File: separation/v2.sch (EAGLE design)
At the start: 6 parts

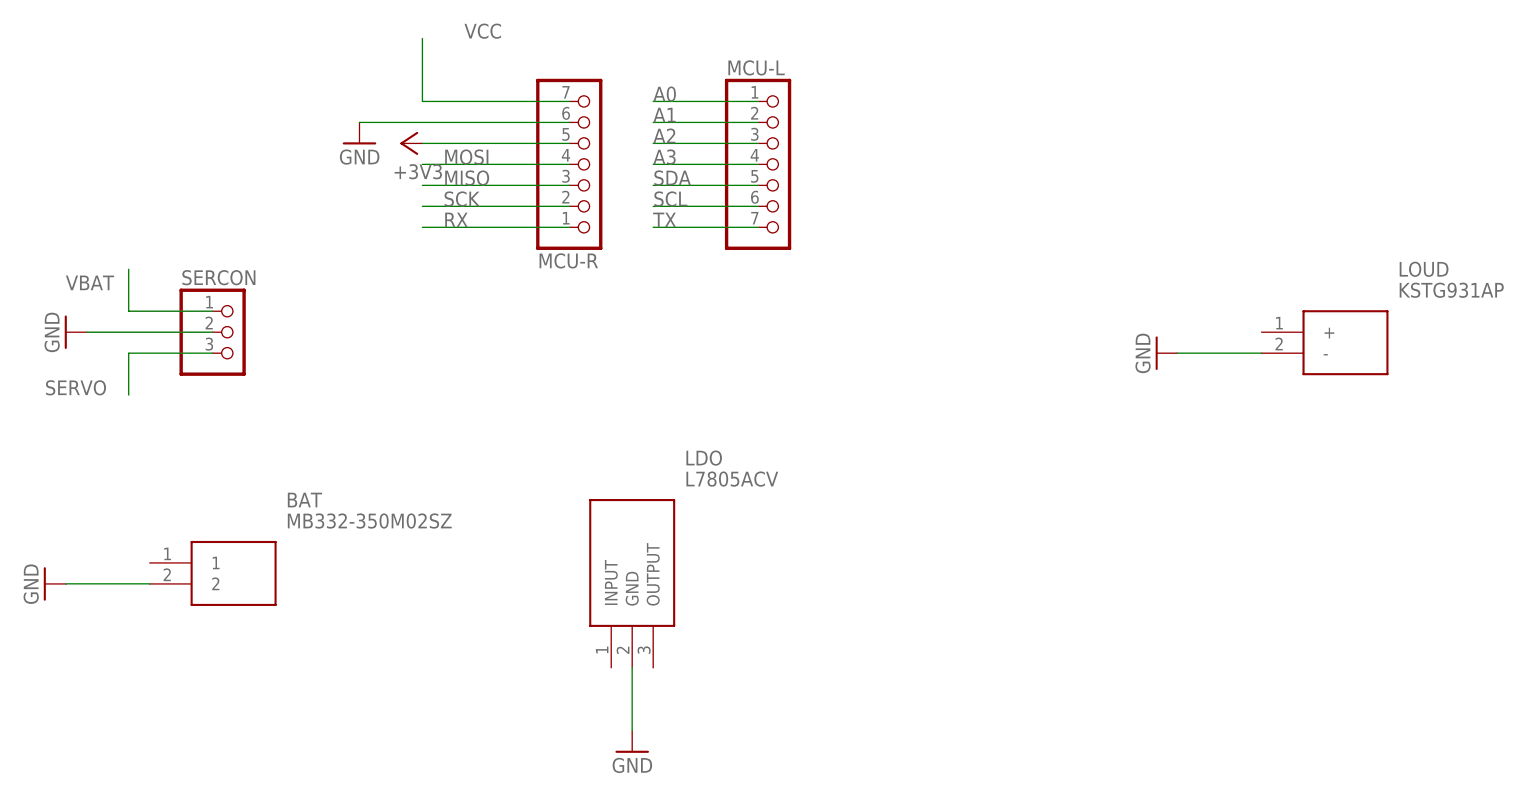
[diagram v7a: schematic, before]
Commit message: connect components to nets
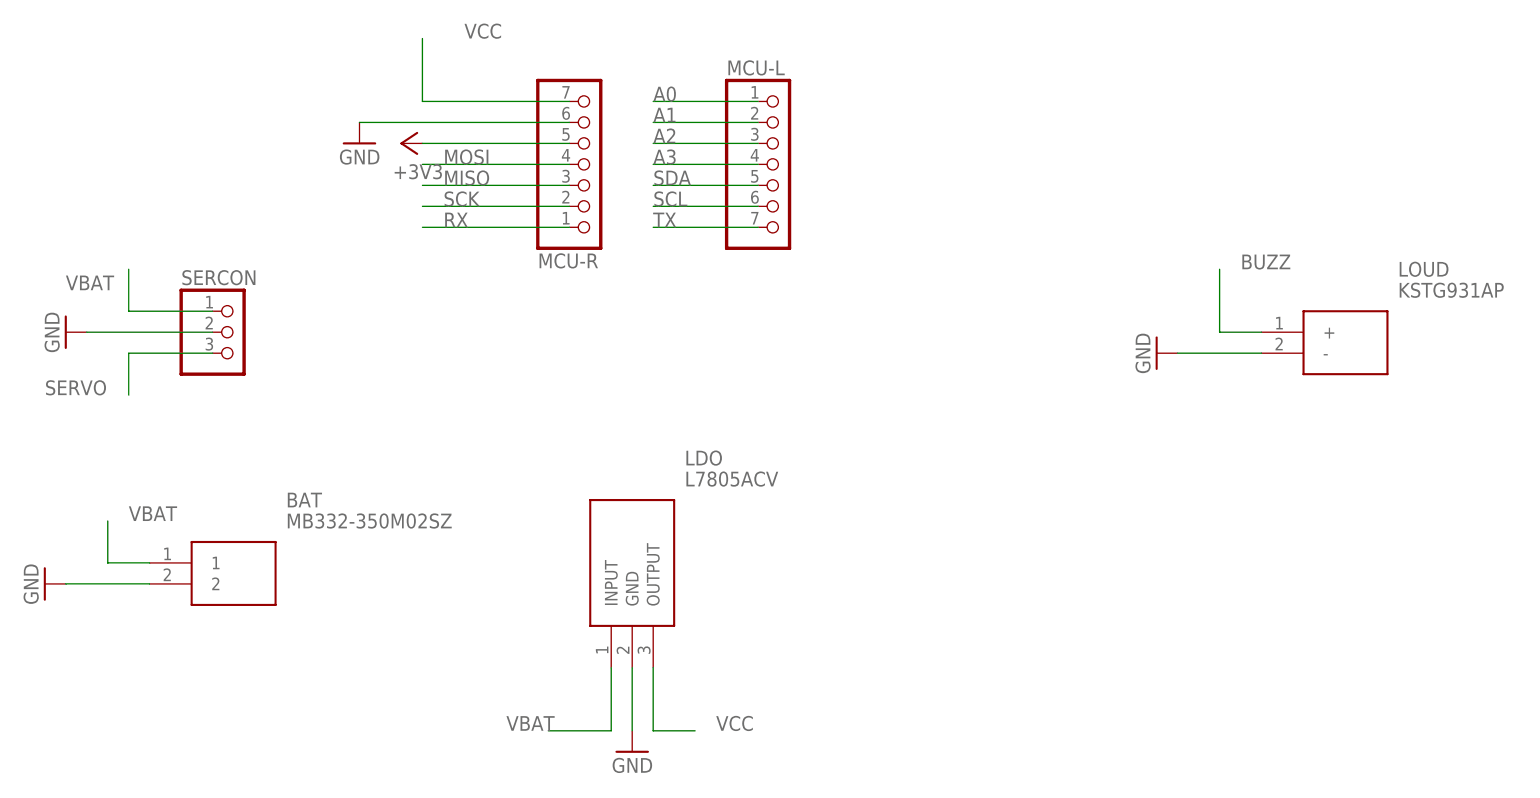
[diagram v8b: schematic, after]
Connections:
- new net BUZZ: LOUD.+
- net VBAT: now also BAT.1, LDO.INPUT
- net VCC: now also LDO.OUTPUT
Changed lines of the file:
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@@
 <label x="22.86" y="73.66" size="1.778" layer="95"/>
+</segment>
+<segment>
+<pinref part="LDO" gate="G$1" pin="OUTPUT"/>
+<wire x1="45.72" y1="-2.54" x2="45.72" y2="-10.16" width="0.1524" layer="91"/>
+<wire x1="45.72" y1="-10.16" x2="50.8" y2="-10.16" width="0.1524" layer="91"/>
+<label x="53.34" y="-10.16" size="1.778" layer="95"/>
 </segment>
 </net>
@@
 <wire x1="-17.78" y1="40.64" x2="-17.78" y2="45.72" width="0.1524" layer="91"/>
 <label x="-25.4" y="43.18" size="1.778" layer="95"/>
+</segment>
+<segment>
+<pinref part="BAT" gate="G$1" pin="1"/>
+<wire x1="-15.24" y1="10.16" x2="-20.32" y2="10.16" width="0.1524" layer="91"/>
+<wire x1="-20.32" y1="10.16" x2="-20.32" y2="15.24" width="0.1524" layer="91"/>
+<label x="-17.78" y="15.24" size="1.778" layer="95"/>
+</segment>
+<segment>
+<pinref part="LDO" gate="G$1" pin="INPUT"/>
+<wire x1="40.64" y1="-2.54" x2="40.64" y2="-10.16" width="0.1524" layer="91"/>
+<wire x1="40.64" y1="-10.16" x2="33.02" y2="-10.16" width="0.1524" layer="91"/>
+<label x="27.94" y="-10.16" size="1.778" layer="95"/>
 </segment>
 </net>
@@
 </segment>
 </net>
+<net name="BUZZ" class="0">
+<segment>
+<pinref part="LOUD" gate="G$1" pin="+"/>
+<wire x1="119.38" y1="38.1" x2="114.3" y2="38.1" width="0.1524" layer="91"/>
+<wire x1="114.3" y1="38.1" x2="114.3" y2="45.72" width="0.1524" layer="91"/>
+<label x="116.84" y="45.72" size="1.778" layer="95"/>
+</segment>
+</net>
